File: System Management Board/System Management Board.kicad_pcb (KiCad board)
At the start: 4 copper layers, 150 x 110 mm, 130 parts, among them IC1 SI2318CDS-T1-GE3, IC2 SI2318CDS-T1-GE3, IC3 SI2318CDS-T1-GE3, IC4 SI2318CDS-T1-GE3, IC5 SI2318CDS-T1-GE3, IC6 SI2318CDS-T1-GE3, J1 Conn_01x04_Male, J10 Conn_01x02_Male, J11 Conn_02x20_Odd_Even, J12 Conn_02x05_Top_Bottom, J13 Conn_01x04_Female, J2 Conn_01x04_Male, J3 Conn_01x02_Male, J4 PJ-063BH, J5 Conn_01x02_Male, J6 Conn_02x06_Counter_Clockwise, J7 Conn_02x20_Odd_Even, J8 Conn_01x02_Male, J9 Conn_01x02_Male, K1 J115F11CH5VDCS61.5U, K2 J114FL1CS165VDC.41, K3 J114FL1CS165VDC.41, SW1 SW_Push, SW2 SW_Push, U1 SC0915, U2 OKI-78SR-5/1.5-W36E-C, U3 OKI-78SR-5/1.5-W36E-C, U4 AP7375-50W5-7, U5 74HC4051, U6 MCP9700T-ETT, U7 MCP9700T-ETT

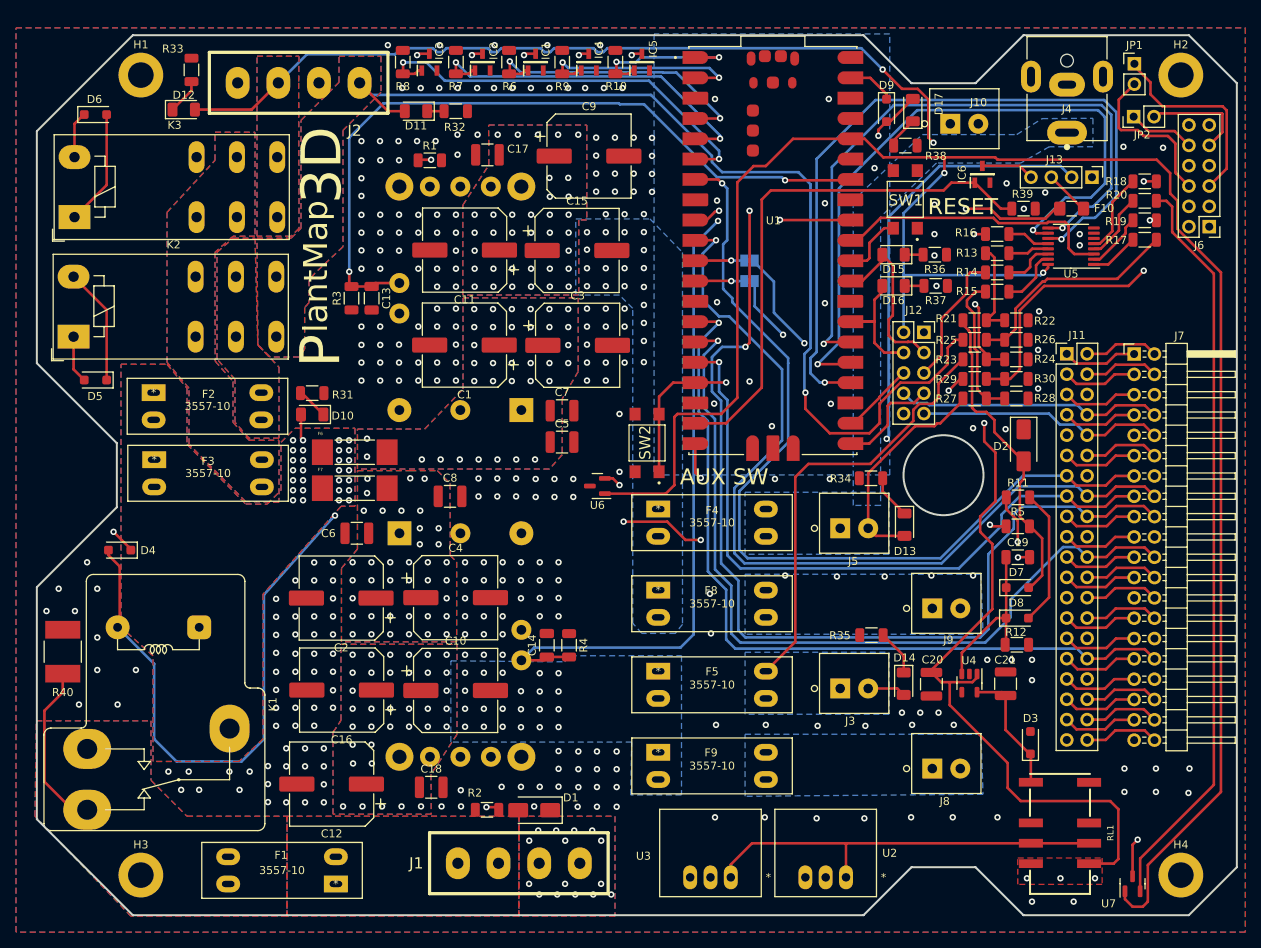
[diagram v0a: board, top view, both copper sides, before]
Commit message: initial commit of THT Pi Pico Board
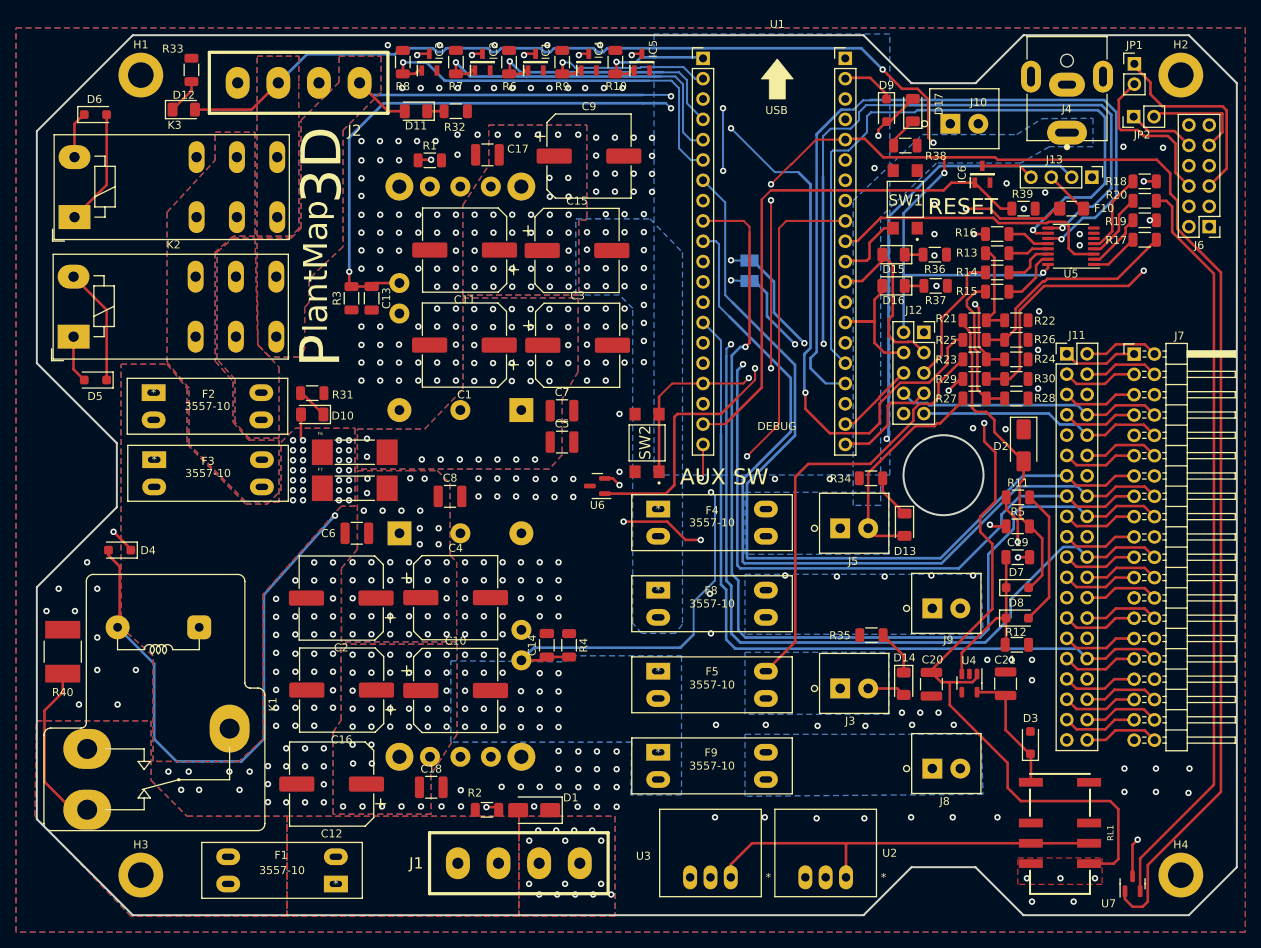
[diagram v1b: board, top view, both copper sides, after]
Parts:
- R23: value 100k -> 220k
- R5: value 10k -> 28
- U1: footprint SMB:MODULE_SC0915 -> SMB:MODULE_SCO915_Custom_HeaderStyle
- moved U1 26.7 mm to (156.1, 47.4)
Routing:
- net /PICO OUT BIT 2: track 132.0 -> 125.5 mm, vias 3 -> 1
- net /POE SW PWR CM: track 98.0 -> 92.7 mm
- net /SWITCH PWR EN: track 20.0 -> 15.1 mm, vias 2 -> 1
- net /COMP PWR EN: track 27.2 -> 22.4 mm, vias 2 -> 1
- net /PICO IN BIT 1: track 100.6 -> 96.3 mm, vias 1 -> 0
- net /Aux_SW: track 101.2 -> 97.5 mm
- net /Main Relay EN: track 36.5 -> 32.8 mm, vias 2 -> 1
- net /Jet_UART1_Rx: track 63.7 -> 66.8 mm
- net /PICO IN BIT 0: track 108.2 -> 105.1 mm, vias 1 -> 0
- net /MUX_S2: track 83.7 -> 86.6 mm
- net /PICO OUT BIT 1: track 110.8 -> 108.1 mm, vias 1 -> 0
- net /PICO 3V3: track 256.5 -> 254.4 mm, vias 2 -> 6
- net /Light A Relay EN: track 44.3 -> 42.4 mm, vias 2 -> 1
- net /Analog Mux OUT: track 34.3 -> 36.0 mm
- net /Jet_UART1_Tx: track 59.7 -> 61.2 mm
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
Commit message: fixed a missing connection, route spacing between THT, and 3D model compatibility
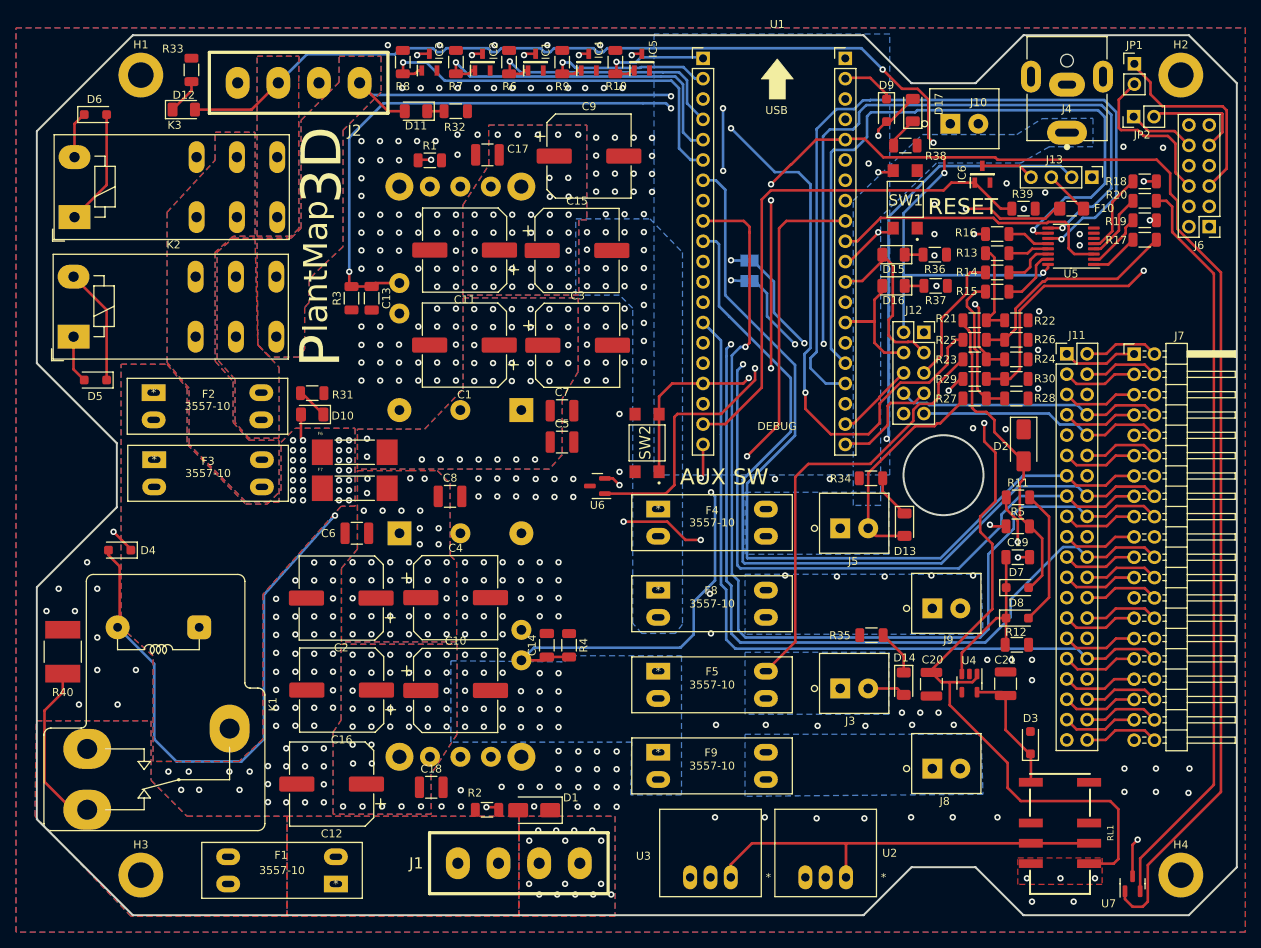
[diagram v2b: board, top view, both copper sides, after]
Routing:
- net Net-(U1-~{RUN}): track 8.16 -> 16.7 mm, vias 0 -> 2
- net /PICO OUT BIT 1: track 108.1 -> 109.0 mm

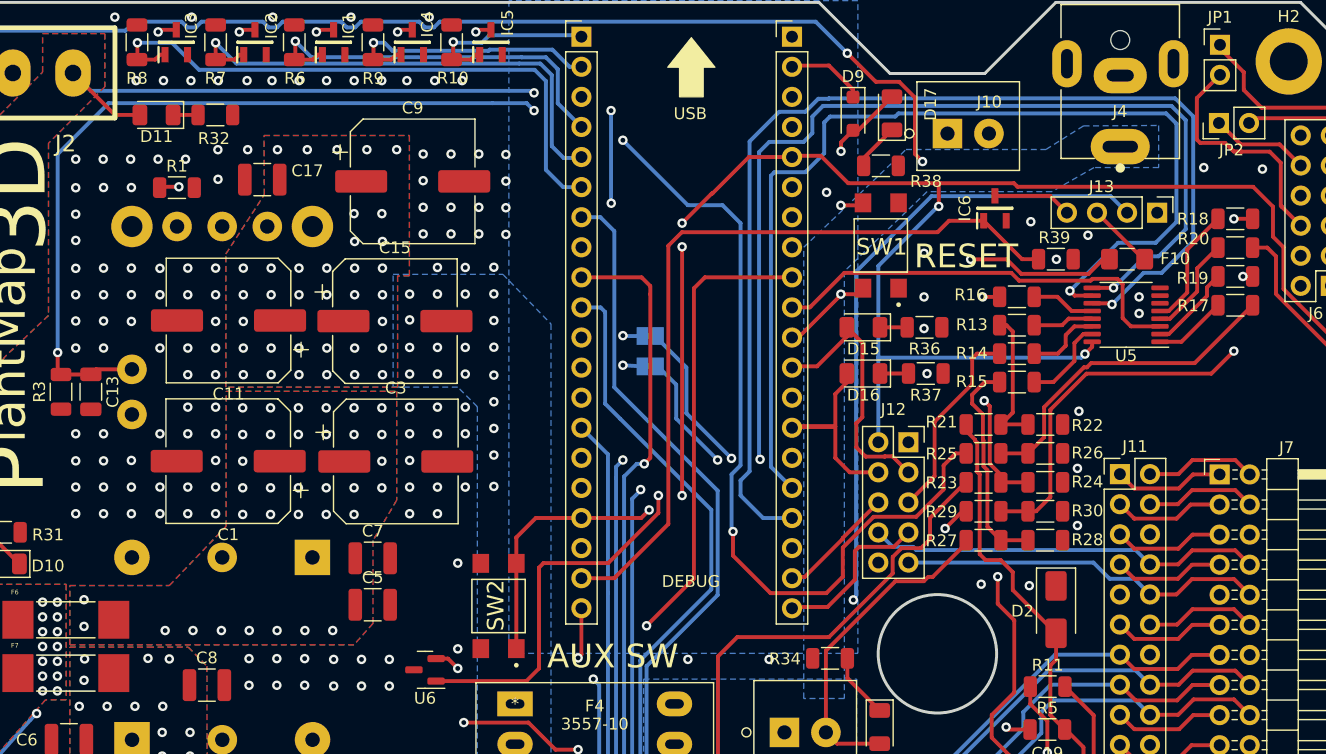
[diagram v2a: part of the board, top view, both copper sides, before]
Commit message: route optimization and via reduction
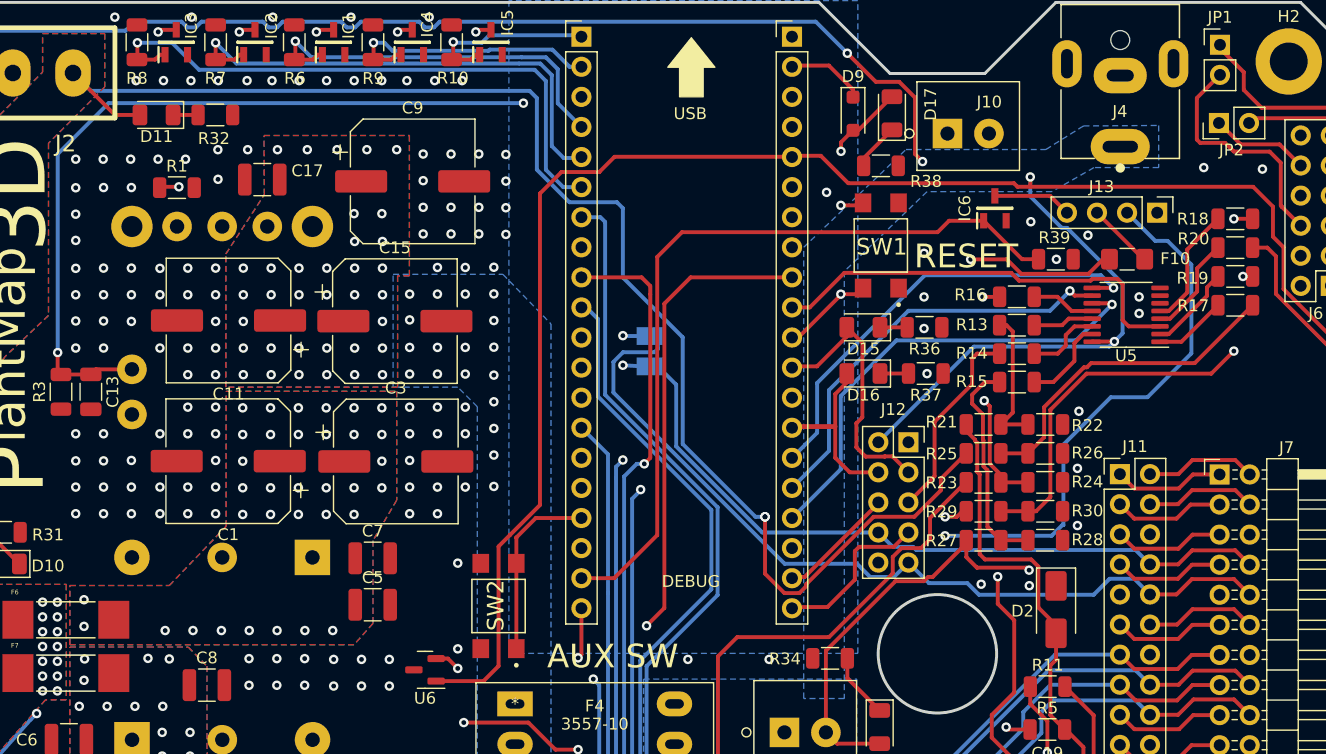
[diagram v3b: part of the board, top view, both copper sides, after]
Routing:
- net /MUX_S0: track 96.3 -> 39.8 mm
- net /MUX_S1: track 87.1 -> 35.4 mm
- net /COMP PWR OUT PROT: track 27.4 -> 76.4 mm, vias 0 -> 1
- net /MUX_S2: track 86.8 -> 38.2 mm, vias 2 -> 1
- net /Jet_UART1_Rx: track 66.8 -> 71.9 mm, vias 1 -> 0
- net /LIGHT BANK A PROT SW: track 125.7 -> 121.3 mm, vias 3 -> 2
- net /TEMP_SENSE_1: track 126.0 -> 129.5 mm, vias 4 -> 2
- net /PICO 3V3: track 254.4 -> 257.3 mm, vias 6 -> 2
- net /Aux_SW: track 97.5 -> 100.0 mm, vias 2 -> 1
- net /V_batt+ PROT: track 230.9 -> 232.7 mm
- net /KeySwitch IN: track 39.2 -> 40.8 mm
- net /LIGHT BANK B PROT SW: track 138.6 -> 137.2 mm
- net /PICO IN BIT 0: track 105.1 -> 104.4 mm
- net /POE SW PWR CM: track 92.7 -> 93.4 mm
- net /Jet_UART1_Tx: track 61.4 -> 60.9 mm, vias 1 -> 0
